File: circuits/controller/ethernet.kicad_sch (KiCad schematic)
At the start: 29 parts, among them Q9 Q_LMUN2211LT1G, U15 LAN8720A

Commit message: sent to fab! 0.6
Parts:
- removed C29, C30, C33: C_22uF, Capacitor_SMD:C_0603_1608Metric_Pad1.08x0.95mm_HandSolder, symbol Open_Automation:C_22uF
- removed C31, C32, C35, C36, C38: C_100nF_0402, Capacitor_SMD:C_0402_1005Metric_Pad0.74x0.62mm_HandSolder, symbol Open_Automation:C_100nF_0402
- removed C34: C_10uF, Capacitor_SMD:C_0805_2012Metric_Pad1.18x1.45mm_HandSolder, symbol Open_Automation:C_10uF
- removed C37: C_2.2uF_0402, Capacitor_SMD:C_0402_1005Metric_Pad0.74x0.62mm_HandSolder, symbol Open_Automation:C_2.2uF_0402
- removed FET1: PFET, Package_TO_SOT_SMD:SOT-23, symbol Open_Automation:PFET
- removed L2: FB, Inductor_SMD:L_1206_3216Metric, symbol Open_Automation:FB
- removed Q9: Q_LMUN2211LT1G, Package_TO_SOT_SMD:SOT-23, symbol Open_Automation:Q_LMUN2211LT1G
- removed R3, R90, R91, R93: 2.2K, Resistor_SMD:R_0402_1005Metric_Pad0.72x0.64mm_HandSolder, symbol Open Automation:R_2.2K
- removed R67, R76: R_10K_0402, Resistor_SMD:R_0402_1005Metric_Pad0.72x0.64mm_HandSolder, symbol Open_Automation:R_10K_0402
- removed R68: R_1K_0402, Resistor_SMD:R_0402_1005Metric_Pad0.72x0.64mm_HandSolder, symbol Open_Automation:R_1K_0402
- removed R69, R71, R72, R73: R_49.9_0402, Resistor_SMD:R_0402_1005Metric_Pad0.72x0.64mm_HandSolder, symbol Open_Automation:R_49.9_0402
- removed R70: R_12.1K_0402, Resistor_SMD:R_0402_1005Metric_Pad0.72x0.64mm_HandSolder, symbol Open_Automation:R_12.1K_0402
- removed R74, R75: R_2K2_0402, Resistor_SMD:R_0402_1005Metric_Pad0.72x0.64mm_HandSolder, symbol Open_Automation:R_2K2_0402
- removed R92: ~, Resistor_SMD:R_0402_1005Metric_Pad0.72x0.64mm_HandSolder, symbol Open Automation:R_2.2K
- removed U15: LAN8720A, Package_DFN_QFN:QFN-24-1EP_4x4mm_P0.5mm_EP2.6x2.6mm, symbol Interface_Ethernet:LAN8720A
- added D14, D15, D16, D17: Red, LED_SMD:LED_0603_1608Metric, symbol open_automation:LED-0603-R
- added J17: CONN_RJ45, Connector_RJ:RJ45_Amphenol_RJHSE538X, symbol open_automation:CONN_RJ45
- added R5 (x2): 10K, Resistor_SMD:R_0402_1005Metric_Pad0.72x0.64mm_HandSolder, symbol Open_Automation:R_10K_0402
- added R69, R70, R71, R72, R73: 1K, Resistor_SMD:R_0402_1005Metric_Pad0.72x0.64mm_HandSolder, symbol open_automation:R_1K_0402
- added U12: W5500, Package_QFP:LQFP-48_7x7mm_P0.5mm, symbol open_automation:W5500
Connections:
- net 3V3: now also R5.2, R69.2, U12.11 (AVDD), U12.15 (AVDD), U12.17 (AVDD), U12.21 (AVDD), U12.28 (VDD), U12.4 (AVDD), U12.43 (PMODE2), U12.8 (AVDD)
- net GND: now also J17.11, J17.7, J17.8, J17.9, R70.2, R71.2, R72.2, R73.2, U12.14 (AGND), U12.16 (AGND), U12.19 (AGND), U12.23 (RSVD), U12.29 (GND), U12.3 (AGND), U12.38 (RSVD), U12.39 (RSVD), U12.40 (RSVD), U12.41 (RSVD), U12.42 (RSVD), U12.44 (PMODE1), U12.45 (PMODE0), U12.48 (AGND), U12.9 (AGND)
- new net: J17.10, R5.1
- new net: R69.1, U12.37 (~{RST})
- new net: D14.1 (K), R70.1
- new net: D15.1 (K), R71.1
- new net: J17.12, R5.1
- new net: D17.1 (K), R73.1
- new net: D14.2 (A), U12.24 (SPDLED)
- new net: D15.2 (A), U12.25 (LINKLED)
- new net: D16.2 (A), U12.26 (DUPLED)
- new net: D17.2 (A), U12.27 (ACTLED)
- new net: D16.1 (K), R72.1
- new net CS: U12.32 (~{SCS})
- new net MISO: U12.34 (MISO)
- new net MOSI: U12.35 (MOSI)
- new net POWER: J17.4, J17.5, R5.2
- new net RX_N: J17.6, U12.5 (RXN)
- new net RX_P: J17.3, U12.6 (RXP)
- new net SCLK: U12.33 (SCLK)
- new net TX_N: J17.2, U12.1 (TXN)
- new net TX_P: J17.1, U12.2 (TXP)
- no-connect marks 2 -> 7

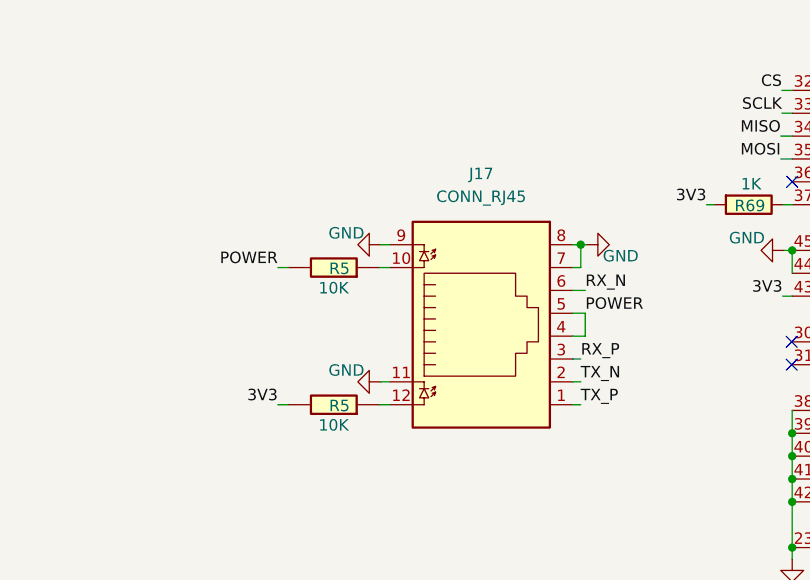
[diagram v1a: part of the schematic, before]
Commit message: Remove obsolete access controller lock file and multiple outdated backup zip files. Enhance automation service with improved logging, including a shutdown handler and better memory management for log persistence. Introduce new API routes for Wiegand state management and update related services for improved functionality and error handling.
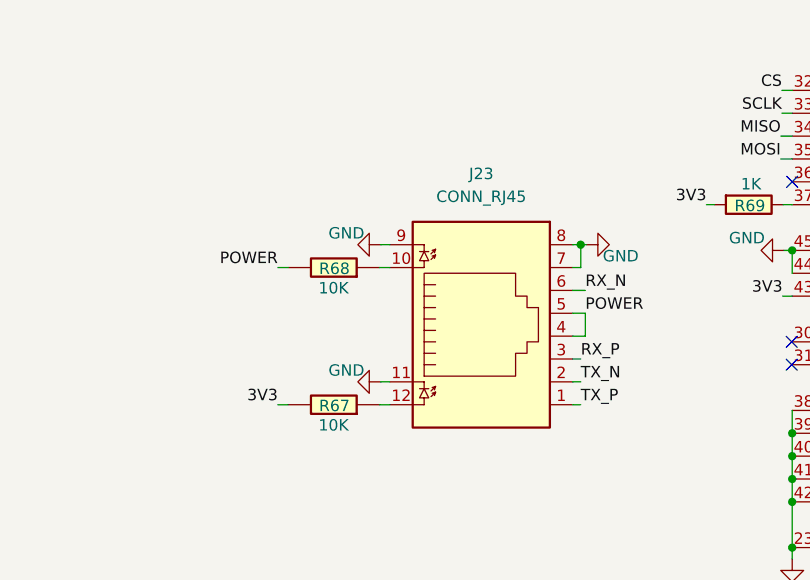
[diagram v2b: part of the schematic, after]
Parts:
- renumbered J17 to J23, R5 to R67, R5 to R68
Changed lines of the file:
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@@
   (symbol (lib_name "R_10K_0402_2") (lib_id "Open_Automation:R_10K_0402") (at 90.8558 88.0872 90) (unit 1)
     (in_bom yes) (on_board yes) (dnp no)
-    (property "Reference" "R5" (at 92.6338 88.2142 90)
+    (property "Reference" "R68" (at 92.6338 88.2142 90)
       (effects (font (size 1.27 1.27)) (justify left))
     )
@@
     (instances
       (project "access-controller"
-        (path "/89df70f4-3579-42b9-861e-6beb04a3b25e/00000000-0000-0000-0000-00006045445b"
-          (reference "R5") (unit 1)
-        )
         (path "/89df70f4-3579-42b9-861e-6beb04a3b25e/00000000-0000-0000-0000-0000618d2964"
           (reference "R68") (unit 1)
@@
   (symbol (lib_id "power:GND") (at 96.0628 100.7872 270) (unit 1)
     (in_bom yes) (on_board yes) (dnp no)
-    (property "Reference" "#PWR02" (at 89.7128 100.7872 0)
+    (property "Reference" "#PWR089" (at 89.7128 100.7872 0)
       (effects (font (size 1.27 1.27)) hide)
     )
@@
     (instances
       (project "access-controller"
-        (path "/89df70f4-3579-42b9-861e-6beb04a3b25e"
-          (reference "#PWR02") (unit 1)
-        )
         (path "/89df70f4-3579-42b9-861e-6beb04a3b25e/00000000-0000-0000-0000-0000618d2964"
           (reference "#PWR089") (unit 1)
@@
   (symbol (lib_id "power:GND") (at 201.041 97.3582 90) (unit 1)
     (in_bom yes) (on_board yes) (dnp no)
-    (property "Reference" "#PWR019" (at 207.391 97.3582 0)
+    (property "Reference" "#PWR093" (at 207.391 97.3582 0)
       (effects (font (size 1.27 1.27)) hide)
     )
@@
     (instances
       (project "access-controller"
-        (path "/89df70f4-3579-42b9-861e-6beb04a3b25e"
-          (reference "#PWR019") (unit 1)
-        )
         (path "/89df70f4-3579-42b9-861e-6beb04a3b25e/00000000-0000-0000-0000-0000618d2964"
           (reference "#PWR093") (unit 1)
@@
   (symbol (lib_id "power:GND") (at 157.0228 125.5522 0) (unit 1)
     (in_bom yes) (on_board yes) (dnp no)
-    (property "Reference" "#PWR019" (at 157.0228 131.9022 0)
+    (property "Reference" "#PWR078" (at 157.0228 131.9022 0)
       (effects (font (size 1.27 1.27)) hide)
     )
@@
     (instances
       (project "access-controller"
-        (path "/89df70f4-3579-42b9-861e-6beb04a3b25e"
-          (reference "#PWR019") (unit 1)
-        )
         (path "/89df70f4-3579-42b9-861e-6beb04a3b25e/00000000-0000-0000-0000-0000618d2964"
           (reference "#PWR078") (unit 1)
@@
   (symbol (lib_id "power:GND") (at 200.8378 105.4862 90) (unit 1)
     (in_bom yes) (on_board yes) (dnp no)
-    (property "Reference" "#PWR019" (at 207.1878 105.4862 0)
+    (property "Reference" "#PWR094" (at 207.1878 105.4862 0)
       (effects (font (size 1.27 1.27)) hide)
     )
@@
     (instances
       (project "access-controller"
-        (path "/89df70f4-3579-42b9-861e-6beb04a3b25e"
-          (reference "#PWR019") (unit 1)
-        )
         (path "/89df70f4-3579-42b9-861e-6beb04a3b25e/00000000-0000-0000-0000-0000618d2964"
           (reference "#PWR094") (unit 1)
@@
   (symbol (lib_id "power:GND") (at 141.7828 120.4722 0) (unit 1)
     (in_bom yes) (on_board yes) (dnp no)
-    (property "Reference" "#PWR019" (at 141.7828 126.8222 0)
+    (property "Reference" "#PWR091" (at 141.7828 126.8222 0)
       (effects (font (size 1.27 1.27)) hide)
     )
@@
     (instances
       (project "access-controller"
-        (path "/89df70f4-3579-42b9-861e-6beb04a3b25e"
-          (reference "#PWR019") (unit 1)
-        )
         (path "/89df70f4-3579-42b9-861e-6beb04a3b25e/00000000-0000-0000-0000-0000618d2964"
           (reference "#PWR091") (unit 1)
@@
   (symbol (lib_id "power:GND") (at 96.0628 85.5472 270) (unit 1)
     (in_bom yes) (on_board yes) (dnp no)
-    (property "Reference" "#PWR02" (at 89.7128 85.5472 0)
+    (property "Reference" "#PWR090" (at 89.7128 85.5472 0)
       (effects (font (size 1.27 1.27)) hide)
     )
@@
     (instances
       (project "access-controller"
-        (path "/89df70f4-3579-42b9-861e-6beb04a3b25e"
-          (reference "#PWR02") (unit 1)
-        )
         (path "/89df70f4-3579-42b9-861e-6beb04a3b25e/00000000-0000-0000-0000-0000618d2964"
           (reference "#PWR090") (unit 1)
@@
   (symbol (lib_id "open_automation:CONN_RJ45") (at 107.2388 95.7072 0) (unit 1)
     (in_bom yes) (on_board yes) (dnp no) (fields_autoplaced)
-    (property "Reference" "J17" (at 107.2388 77.6732 0)
+    (property "Reference" "J23" (at 107.2388 77.6732 0)
       (effects (font (size 1.27 1.27)))
     )
@@
     (instances
       (project "access-controller"
-        (path "/89df70f4-3579-42b9-861e-6beb04a3b25e"
-          (reference "J17") (unit 1)
-        )
         (path "/89df70f4-3579-42b9-861e-6beb04a3b25e/00000000-0000-0000-0000-0000618d2964"
           (reference "J23") (unit 1)
@@
   (symbol (lib_id "power:GND") (at 200.8886 113.157 90) (unit 1)
     (in_bom yes) (on_board yes) (dnp no)
-    (property "Reference" "#PWR019" (at 207.2386 113.157 0)
+    (property "Reference" "#PWR095" (at 207.2386 113.157 0)
       (effects (font (size 1.27 1.27)) hide)
     )
@@
     (instances
       (project "access-controller"
-        (path "/89df70f4-3579-42b9-861e-6beb04a3b25e"
-          (reference "#PWR019") (unit 1)
-        )
         (path "/89df70f4-3579-42b9-861e-6beb04a3b25e/00000000-0000-0000-0000-0000618d2964"
           (reference "#PWR095") (unit 1)
@@
   (symbol (lib_name "R_10K_0402_2") (lib_id "Open_Automation:R_10K_0402") (at 90.8558 103.3272 90) (unit 1)
     (in_bom yes) (on_board yes) (dnp no)
-    (property "Reference" "R5" (at 92.6338 103.4542 90)
+    (property "Reference" "R67" (at 92.6338 103.4542 90)
       (effects (font (size 1.27 1.27)) (justify left))
     )
@@
     (instances
       (project "access-controller"
-        (path "/89df70f4-3579-42b9-861e-6beb04a3b25e/00000000-0000-0000-0000-00006045445b"
-          (reference "R5") (unit 1)
-        )
         (path "/89df70f4-3579-42b9-861e-6beb04a3b25e/00000000-0000-0000-0000-0000618d2964"
           (reference "R67") (unit 1)
@@
   (symbol (lib_id "power:GND") (at 140.8684 86.1822 270) (unit 1)
     (in_bom yes) (on_board yes) (dnp no)
-    (property "Reference" "#PWR019" (at 134.5184 86.1822 0)
+    (property "Reference" "#PWR096" (at 134.5184 86.1822 0)
       (effects (font (size 1.27 1.27)) hide)
     )
@@
     (instances
       (project "access-controller"
-        (path "/89df70f4-3579-42b9-861e-6beb04a3b25e"
-          (reference "#PWR019") (unit 1)
-        )
         (path "/89df70f4-3579-42b9-861e-6beb04a3b25e/00000000-0000-0000-0000-0000618d2964"
           (reference "#PWR096") (unit 1)
@@
   (symbol (lib_id "power:GND") (at 200.9902 89.8398 90) (unit 1)
     (in_bom yes) (on_board yes) (dnp no)
-    (property "Reference" "#PWR019" (at 207.3402 89.8398 0)
+    (property "Reference" "#PWR092" (at 207.3402 89.8398 0)
       (effects (font (size 1.27 1.27)) hide)
     )
@@
     (instances
       (project "access-controller"
-        (path "/89df70f4-3579-42b9-861e-6beb04a3b25e"
-          (reference "#PWR019") (unit 1)
-        )
         (path "/89df70f4-3579-42b9-861e-6beb04a3b25e/00000000-0000-0000-0000-0000618d2964"
           (reference "#PWR092") (unit 1)
@@
   (symbol (lib_id "power:GND") (at 118.9228 85.5472 90) (unit 1)
     (in_bom yes) (on_board yes) (dnp no)
-    (property "Reference" "#PWR02" (at 125.2728 85.5472 0)
+    (property "Reference" "#PWR077" (at 125.2728 85.5472 0)
       (effects (font (size 1.27 1.27)) hide)
     )
@@
     (instances
       (project "access-controller"
-        (path "/89df70f4-3579-42b9-861e-6beb04a3b25e"
-          (reference "#PWR02") (unit 1)
-        )
         (path "/89df70f4-3579-42b9-861e-6beb04a3b25e/00000000-0000-0000-0000-0000618d2964"
           (reference "#PWR077") (unit 1)
